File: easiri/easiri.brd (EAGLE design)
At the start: 50.8 x 50.8 mm, 46 parts

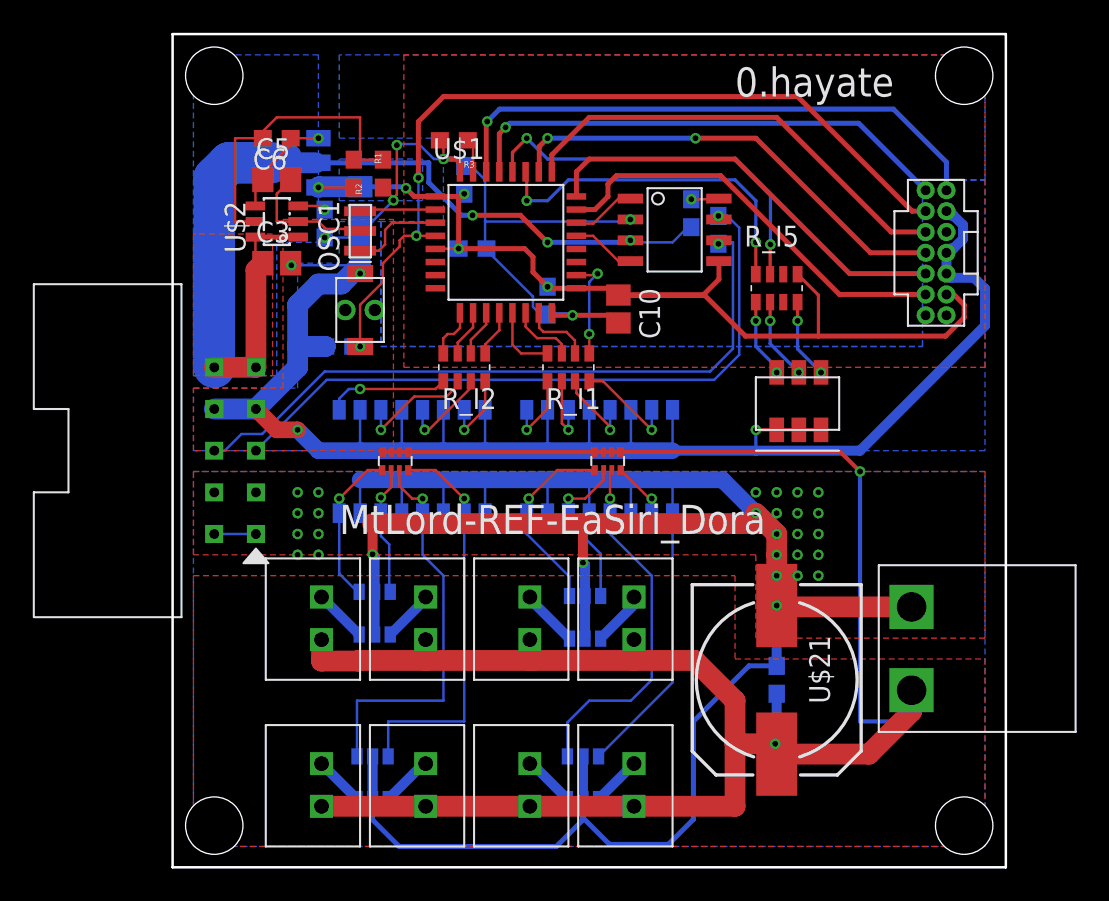
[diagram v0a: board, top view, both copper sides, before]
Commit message: canトランシーバ用のコンデンサを追加
fet駆動にインバッタをはっさんだ。ゲートにledを入れたがそれがそのままプルダウン抵抗に置き換わるかも
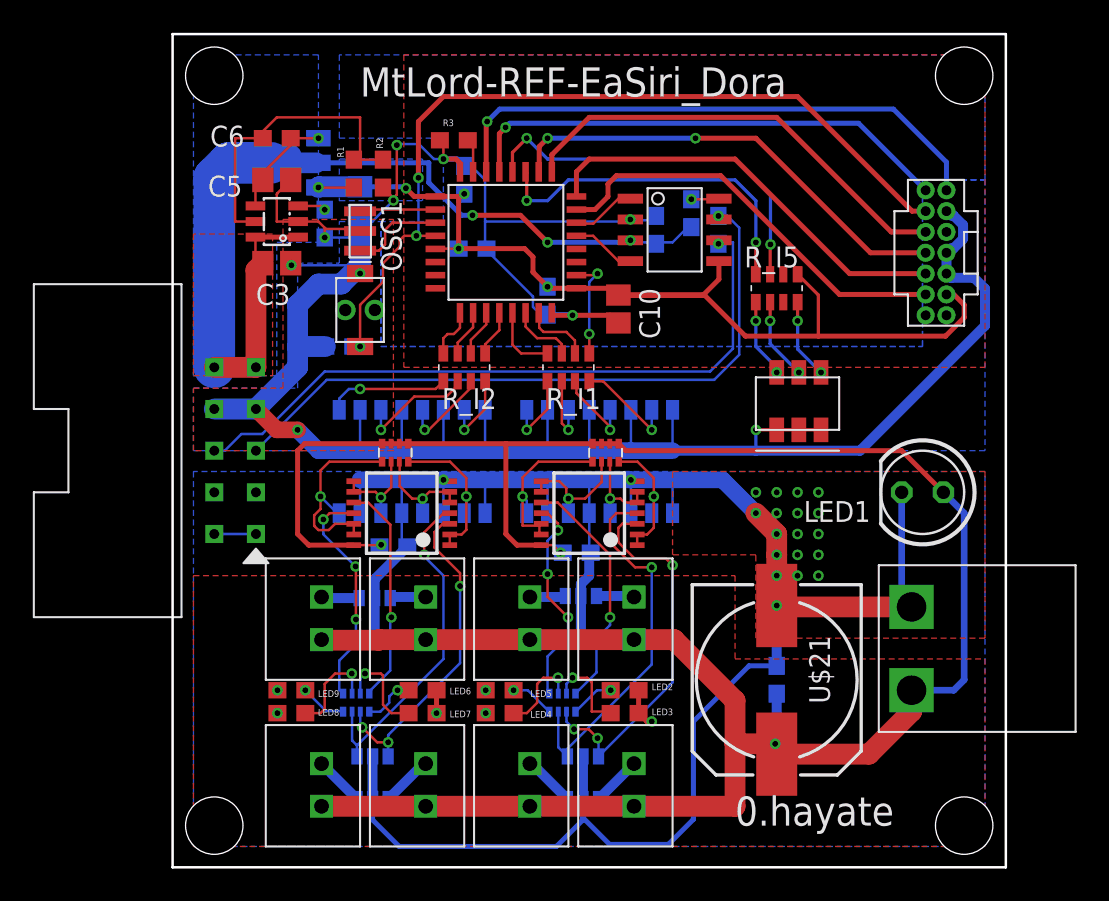
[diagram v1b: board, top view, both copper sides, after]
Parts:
- added C12, C13, C14: 0.1u, rcl:C1608
- added LED1: 抵抗内蔵led, led:LED5MM
- added LED2, LED3, LED4, LED5, LED6, LED7, LED8, LED9: (no value), user_leds:1608
- added NAND1, NAND2: (no value), user_ic:TSSOP14
- added R_I6, R_I7: (no value), user_rcl:1005X4RESISTOR
- R_I3, R_I4: value (none) -> 10k
- moved R_I3 0.52 mm to (25.4, 25.5)
- moved R_I4 0.51 mm to (12.6, 25.5)
- moved U$10 0.38 mm to (12.3, 15.1), turned to 0 degrees
- moved U$8 0.25 mm to (24.9, 15.2), turned to 0 degrees
- renumbered U$13 to ES1, U$14 to ES2, U$15 to ES3, U$16 to ES4, U$17 to ES5, U$18 to ES6, U$19 to ES7, U$20 to ES8
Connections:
- new net N$45: NAND1.4, R_I6.3, U$11.1
- new net N$46: ES5.P$2, U$10.4
- new net N$47: NAND2.8, NAND2.9, R_I3.2, U$6.2_C
- new net N$48: NAND2.1, NAND2.2, R_I3.4, U$6.4_C
- new net N$49: NAND1.12, NAND1.13, R_I4.1, U$7.1_C
- new net N$50: NAND1.10, R_I6.8, U$10.1
- new net N$51: NAND2.3, R_I7.2, U$9.3
- new net N$52: NAND2.4, R_I7.3, U$9.1
- new net N$53: NAND2.10, R_I7.8, U$8.1
- new net N$54: NAND2.11, R_I7.5, U$8.3
- new net N$55: LED9.A, R_I6.4
- new net N$56: LED6.A, R_I6.1
- new net N$57: NAND1.11, R_I6.5, U$10.3
- new net N$58: LED3.A, R_I7.7
- new net N$59: LED5.A, R_I7.4
- new net N$60: LED2.A, R_I7.1
- net GND: now also C14.2
- net GNDA: now also C12.2, C13.2, LED1.K, LED2.K, LED3.K, LED4.K, LED5.K, LED6.K, LED7.K, LED8.K, LED9.K, NAND1.7, NAND2.7
- net N$13: now also NAND2.12, NAND2.13; no longer U$8.1
- net N$17: now also NAND1.5, NAND1.6, R_I4.3, U$7.3_C; no longer R_I3.2, U$6.2_C, U$8.3
- net N$18: now also NAND2.5, NAND2.6; no longer U$9.1
- net N$19: now also NAND1.1, NAND1.2, R_I4.4, U$7.4_C; no longer R_I3.4, U$6.4_C, U$9.3
- net N$20: now also NAND1.3, R_I6.2, U$11.3; no longer R_I4.1, U$10.1, U$7.1_C
- net N$21: now also NAND1.8, NAND1.9; no longer U$10.3
- net N$22: now also LED8.A, R_I6.6; no longer R_I4.3, U$11.1, U$7.3_C
- net N$23: now also LED7.A, R_I6.7; no longer R_I4.4, U$11.3, U$7.4_C
- net N$25: now also U$8.4; no longer U$8.6
- net N$26: now also U$8.6; no longer U$8.4
- net N$28: now also LED4.A, R_I7.6; no longer ES5.P$2, U$10.6
- net N$29: now also U$10.6; no longer U$10.4
- net VCC: now also C14.1
- net VDD: now also C12.1, C13.1, LED1.A, NAND1.14, NAND2.14
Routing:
- net N$51: track 0.00 -> 23.6 mm, vias 0 -> 3
- net N$52: track 0.00 -> 23.0 mm, vias 0 -> 1
- net N$45: track 0.00 -> 20.7 mm, vias 0 -> 1
- net N$23: track 24.5 -> 6.04 mm
- net N$22: track 24.2 -> 5.96 mm
- net N$18: track 22.2 -> 5.55 mm
- net N$53: track 0.00 -> 14.9 mm, vias 0 -> 1
- net N$57: track 0.00 -> 14.2 mm, vias 0 -> 3
- net N$50: track 0.00 -> 13.7 mm, vias 0 -> 1
- net N$54: track 0.00 -> 13.0 mm, vias 0 -> 3
- net N$49: track 0.00 -> 12.6 mm, vias 0 -> 1
- net N$19: track 20.7 -> 9.95 mm
- net N$20: track 9.58 -> 20.2 mm, vias 1 -> 3
- net GNDA: track 141.4 -> 132.1 mm, vias 28 -> 26
- net N$48: track 0.00 -> 8.48 mm, vias 0 -> 1
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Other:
- board text added: "1"
- board text added: "2"
- board text added: "3"
- board text added: "4"
- board text added: "5"
- board text added: "6"
- board text added: "7"
- board text added: "8"

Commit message: ゲートにプルダウン抵抗を追加
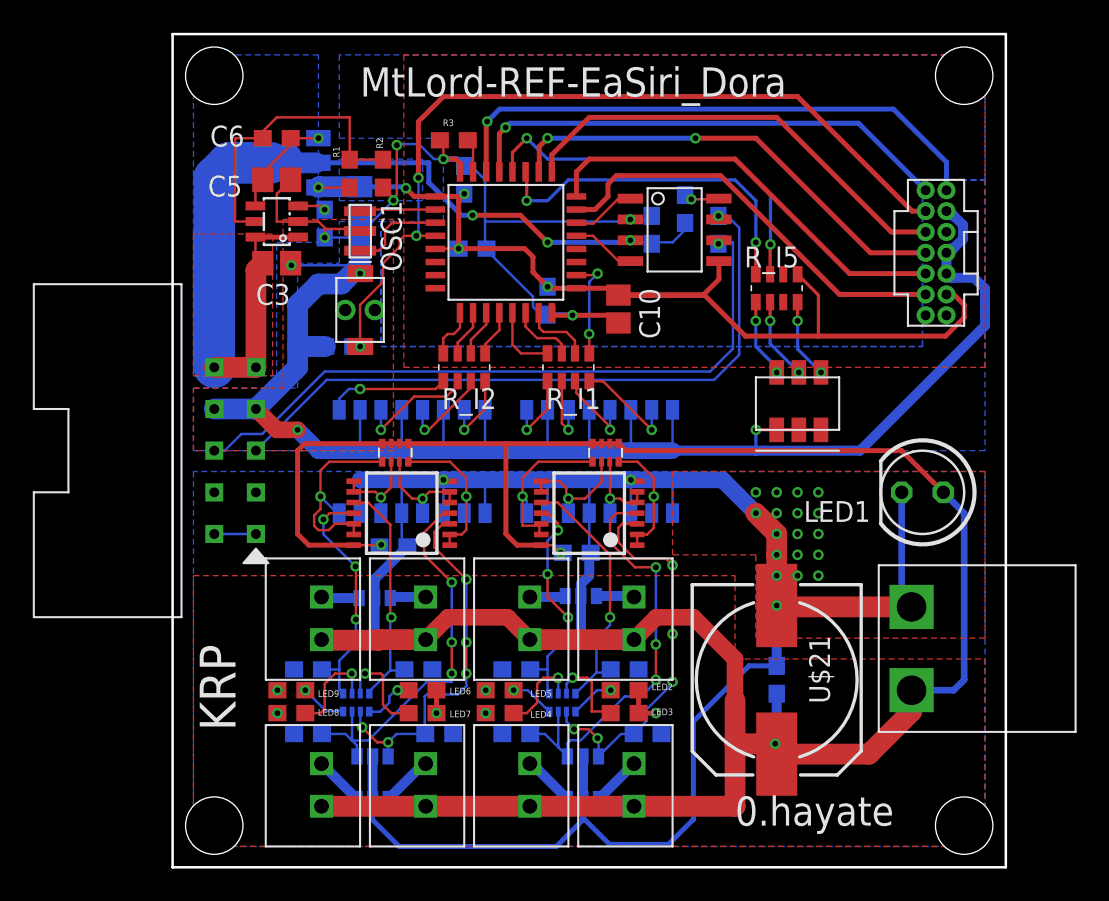
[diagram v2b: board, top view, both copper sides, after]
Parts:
- added R10, R11, R12, R13, R6, R7, R8, R9: 10k, user_rcl:1608
- R_I6, R_I7: value (none) -> 10k
- moved R4 0.46 mm to (31.2, 40.1)
- moved R1 0.25 mm to (10.8, 42.3)
- moved C14 0.25 mm to (29.2, 38.9)
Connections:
- net GNDA: now also R10.1, R11.1, R12.1, R13.1, R6.1, R7.1, R8.1, R9.1
- net N$20: now also R6.2
- net N$45: now also R7.2
- net N$50: now also R9.2
- net N$51: now also R13.2
- net N$52: now also R12.2
- net N$53: now also R10.2
- net N$54: now also R11.2
- net N$57: now also R8.2
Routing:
- net N$45: track 20.7 -> 24.3 mm, vias 1 -> 3
- net VDD: track 151.7 -> 155.3 mm
- net N$52: track 23.0 -> 26.4 mm, vias 1 -> 3
- net N$20: track 20.2 -> 22.7 mm, vias 3 -> 5
- net N$57: track 14.2 -> 15.3 mm
- net N$54: track 13.0 -> 14.0 mm
- net N$53: track 14.9 -> 15.8 mm
- net N$50: track 13.7 -> 14.6 mm
- net N$1: track 19.2 -> 18.7 mm
- net N$51: track 23.6 -> 24.1 mm, vias 3 -> 5

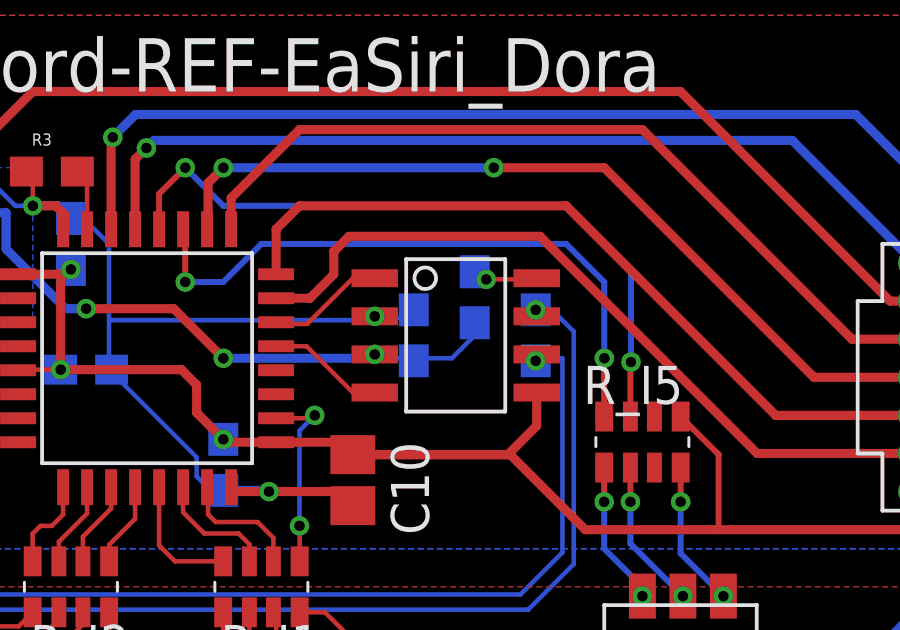
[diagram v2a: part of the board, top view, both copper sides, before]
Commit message: mcp2562スタンバイピンプルダウン
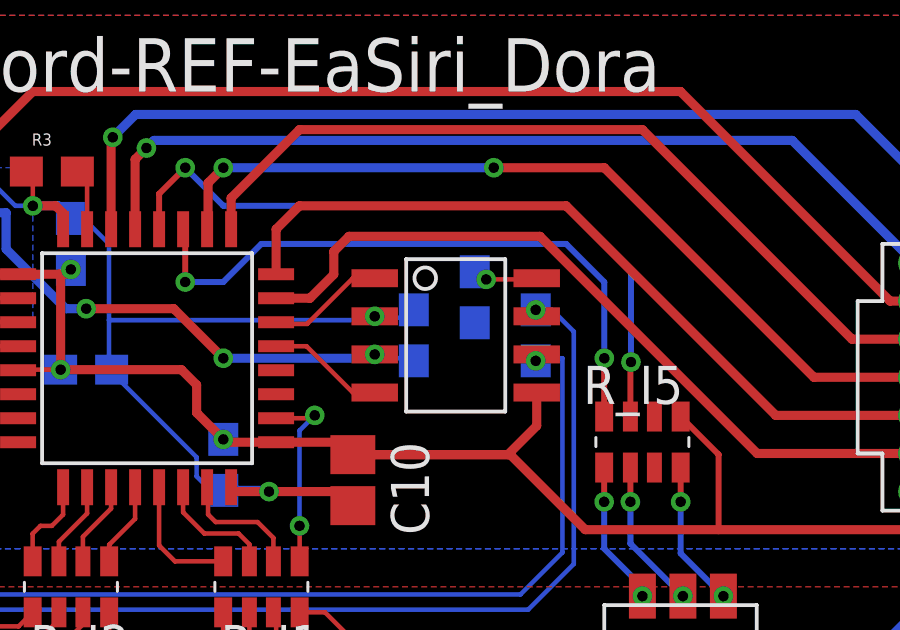
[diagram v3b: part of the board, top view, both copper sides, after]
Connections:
- net GND: now also R4.2
- net VCC: no longer R4.2
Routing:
- net VCC: track 58.1 -> 55.4 mm
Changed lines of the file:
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@@
 <wire x1="29.21" y1="39.712" x2="28.948" y2="39.45" width="0.1524" layer="16"/>
 <wire x1="28.948" y1="39.45" x2="27.86" y2="39.45" width="0.1524" layer="16"/>
+<contactref element="R4" pad="2"/>
 </signal>
 <signal name="VCC">
@@
 <contactref element="BOX10P-L2" pad="P$10"/>
 <contactref element="U$5" pad="P$3"/>
-<contactref element="R4" pad="2"/>
 <wire x1="5.08" y1="30.48" x2="2.54" y2="30.48" width="1.27" layer="1"/>
 <wire x1="5.05" y1="38.42" x2="7.65" y2="38.42" width="0.3048" layer="1"/>
@@
 <wire x1="5.5" y1="36.83" x2="5.05" y2="37.28" width="0.1524" layer="1"/>
 <wire x1="5.05" y1="37.28" x2="5.05" y2="38.42" width="0.1524" layer="1"/>
-<wire x1="31.242" y1="39.282" x2="31.242" y2="38.862" width="0.1524" layer="16"/>
-<wire x1="31.242" y1="38.862" x2="30.48" y2="38.1" width="0.1524" layer="16"/>
-<wire x1="30.48" y1="38.1" x2="29.21" y2="38.1" width="0.1524" layer="16"/>
 <wire x1="29.21" y1="38.1" x2="28.034" y2="38.1" width="0.1524" layer="16"/>
 <wire x1="28.034" y1="38.1" x2="27.907" y2="38.227" width="0.1524" layer="16"/>
@@
 <wire x1="33.268" y1="40.728" x2="31.623" y2="40.728" width="0.1524" layer="1"/>
 <via x="31.623" y="40.728" extent="1-16" drill="0.35"/>
+<wire x1="31.242" y1="40.982" x2="31.369" y2="40.982" width="0.1524" layer="16"/>
+<wire x1="31.369" y1="40.982" x2="31.623" y2="40.728" width="0.1524" layer="16"/>
 </signal>
 <signal name="N$7">
